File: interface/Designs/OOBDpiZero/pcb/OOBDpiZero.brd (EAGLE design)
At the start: 73.5 x 42 mm, 133 parts, among them IC1 LM1117MPX-3.3, IC11 EEPROM24, IC3 DS3231, Q2 12MHz, U1 SN65HVD230(SO8), U2 SN65HVD230(SO8), U3 MAX98357, U4 SY6280, U5 MP1482

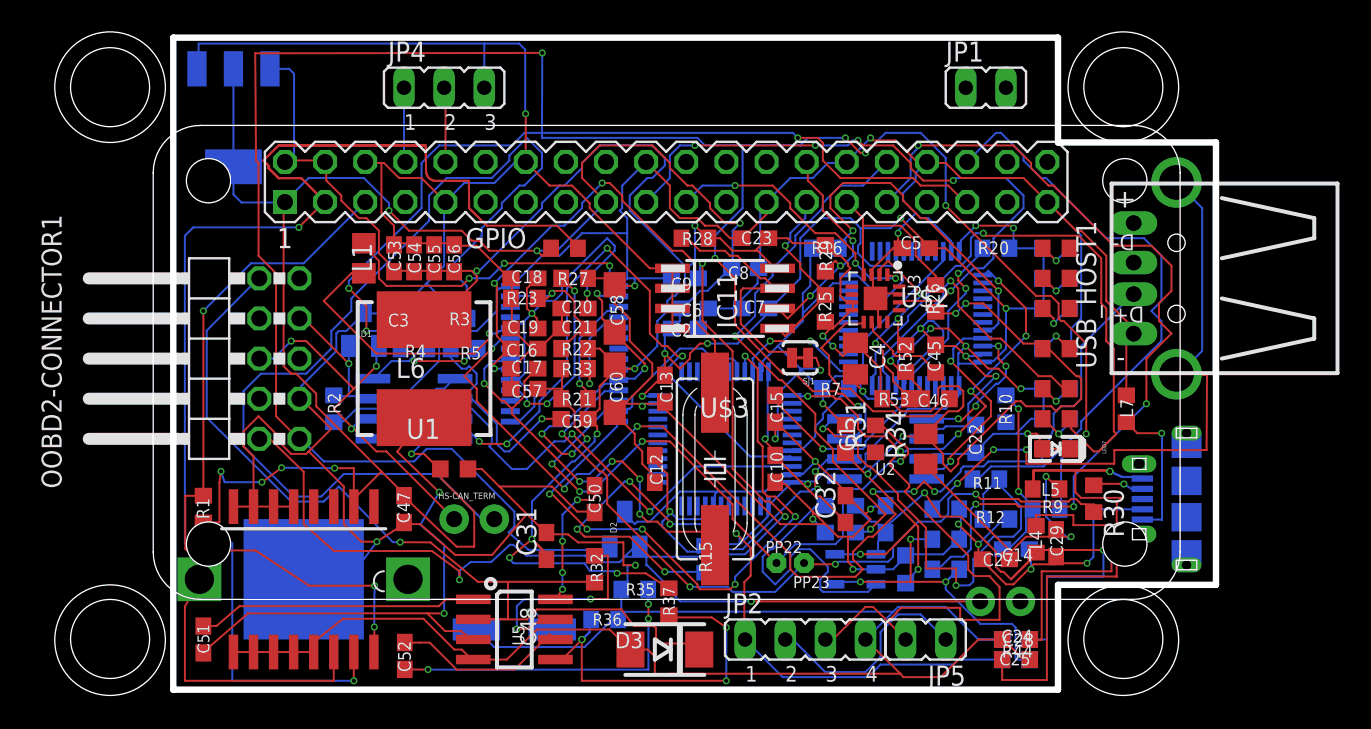
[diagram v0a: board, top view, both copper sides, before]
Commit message: 7 Lines left over, error checking in regards of overlap, distance and restriction done. Mike, please check the restrictions in regards of e.g mounting holes of the pizero pcb
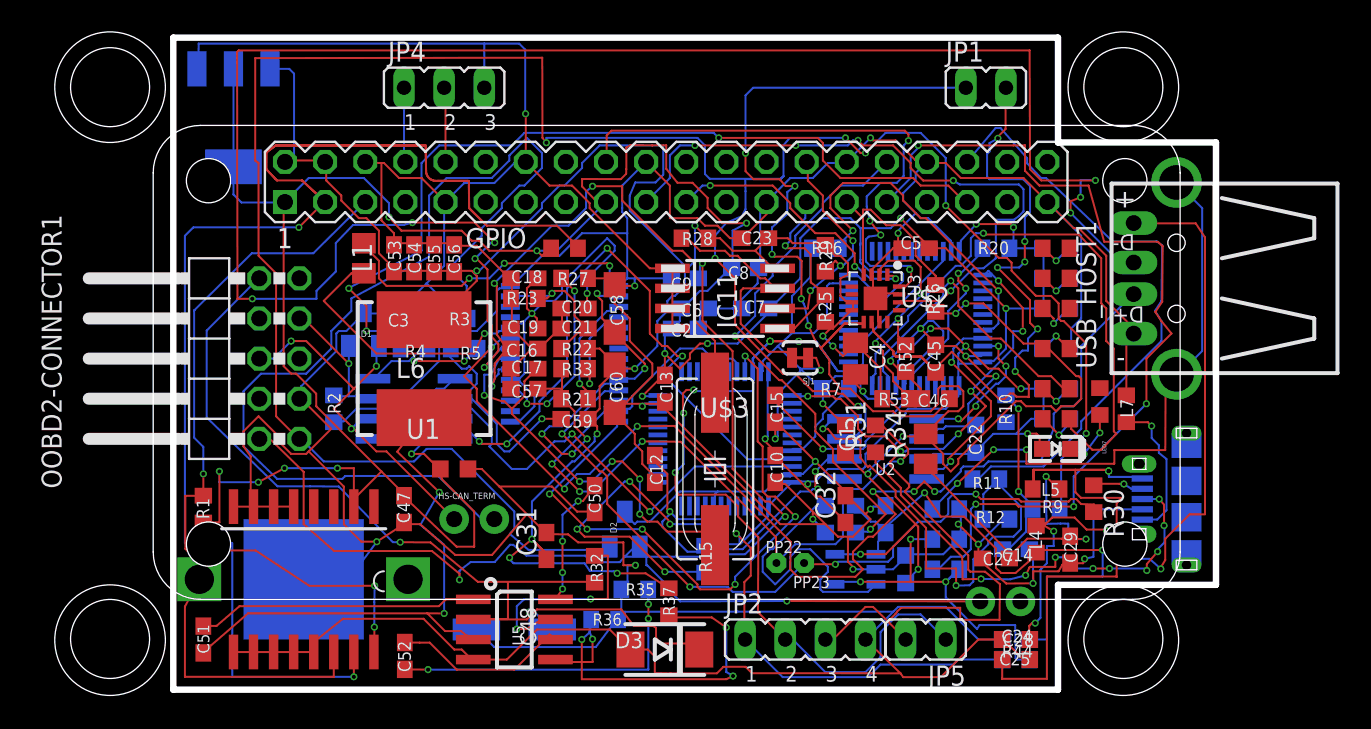
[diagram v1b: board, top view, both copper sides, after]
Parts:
- moved R18 4.08 mm to (58.6, 17.6), turned to 90 degrees
- moved C29 0.98 mm to (56.8, 8.23)
- moved C27 0.05 mm to (52.1, 7.67)
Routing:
- net USB2_DM: track 0.00 -> 118.4 mm, vias 0 -> 8
- net N$3: track 5.80 -> 46.2 mm, vias 0 -> 6
- net N$12: track 14.7 -> 53.4 mm, vias 0 -> 5
- net AUD_BCLK: track 0.00 -> 36.7 mm, vias 0 -> 4
- net SWDIO: track 32.6 -> 66.6 mm, vias 2 -> 7
- net N$43: track 0.00 -> 29.7 mm, vias 0 -> 9
- net N$41: track 18.5 -> 45.9 mm, vias 0 -> 4
- net MS-CAN_H: track 154.6 -> 159.3 mm
- net GND: track 582.3 -> 586.3 mm
- net N$42: track 40.9 -> 37.0 mm
- net +3V3: track 288.1 -> 291.5 mm
- net N$1: track 19.5 -> 21.9 mm
- net N$31: track 34.0 -> 36.4 mm
- net N$26: track 1.74 -> 3.75 mm, vias 0 -> 2
- net USB_CE: track 54.4 -> 56.4 mm
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
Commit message: 6 lines left over, design rule check made
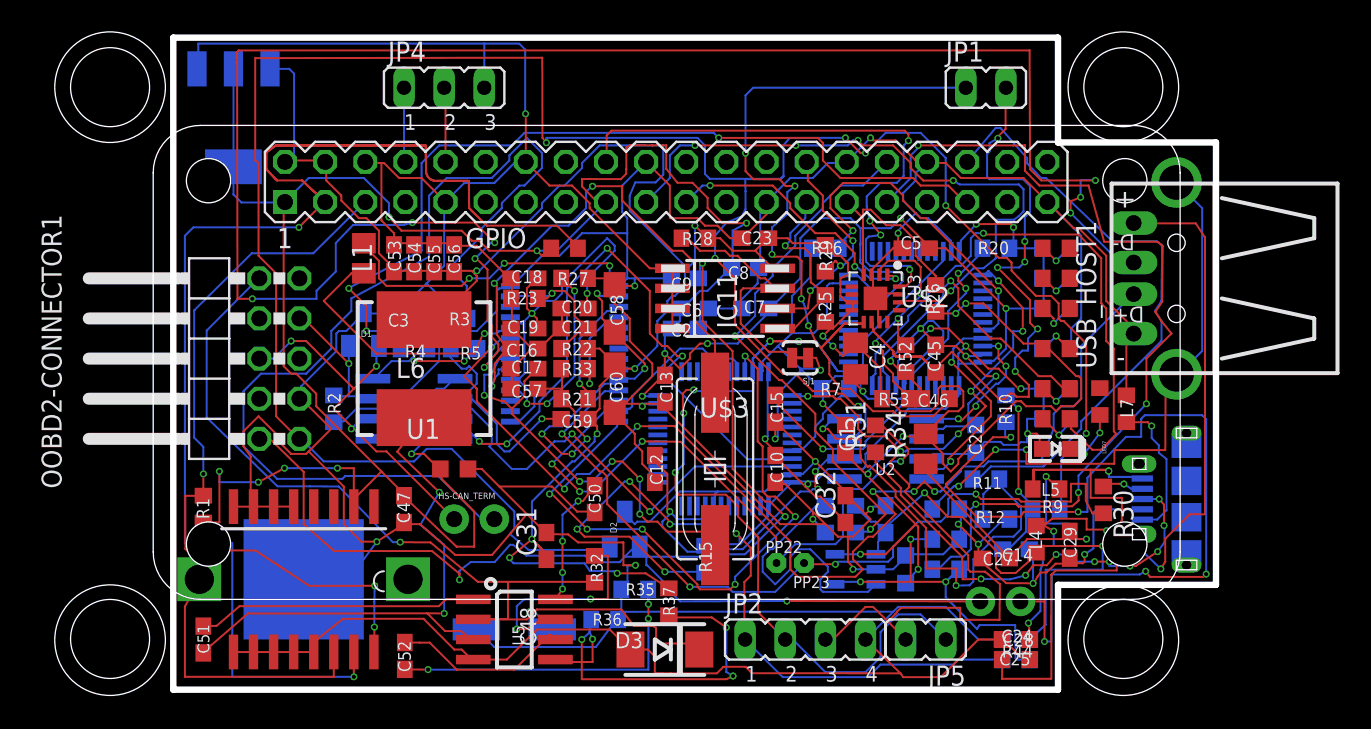
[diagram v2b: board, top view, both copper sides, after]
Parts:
- moved R30 0.61 mm to (58.9, 11.4)
- moved C29 0.31 mm to (56.7, 8.53)
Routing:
- net N$32: track 0.00 -> 57.5 mm, vias 0 -> 5
- net PP23: track 48.0 -> 50.6 mm
- net N$48: track 42.2 -> 41.2 mm
- net +3V3: track 291.5 -> 292.4 mm
- net N$47: track 34.3 -> 33.5 mm
- net N$43: track 29.7 -> 29.0 mm
- net N$38: track 3.22 -> 2.70 mm

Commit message: 4 Lines left, DRC no errors
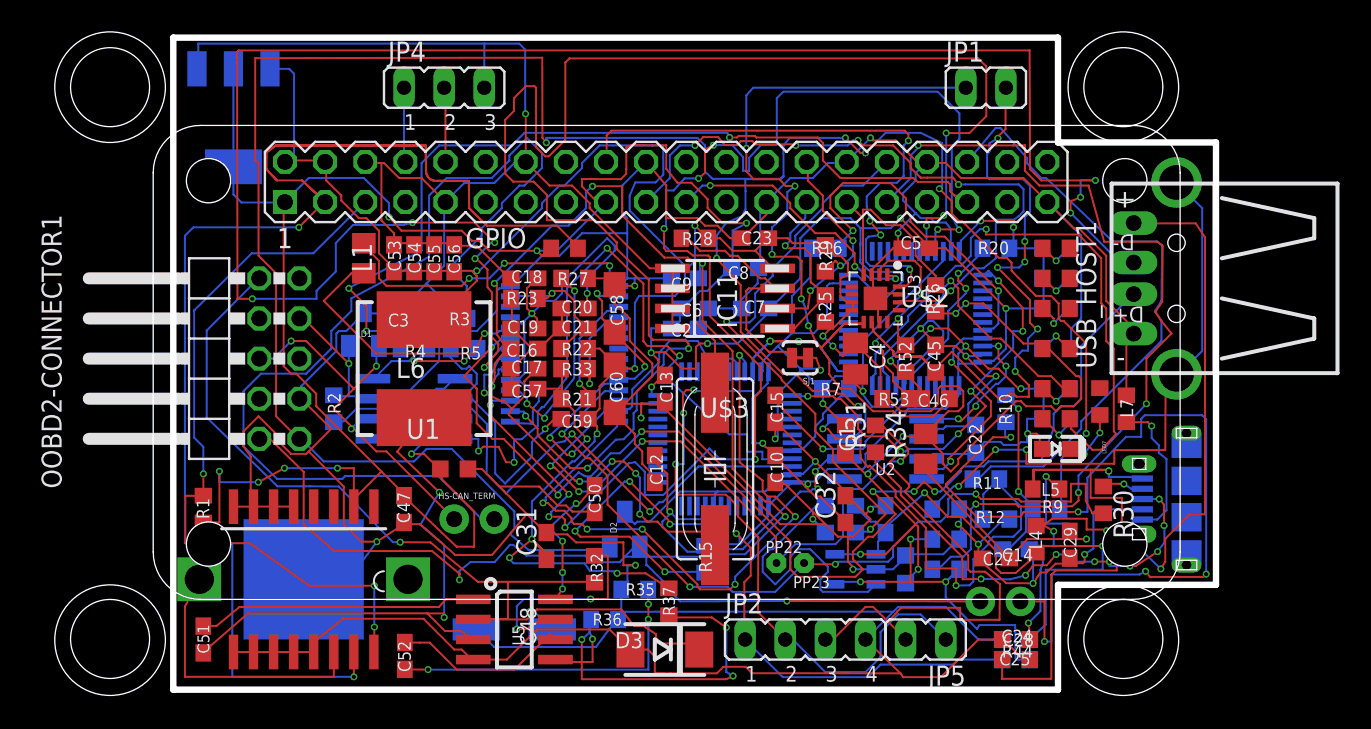
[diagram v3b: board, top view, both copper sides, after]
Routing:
- net USB1_DM: track 0.00 -> 97.2 mm, vias 0 -> 6
- net USB1_DP: track 0.00 -> 88.0 mm, vias 0 -> 10
- net GND: track 586.3 -> 592.7 mm
- net +3V3: track 292.4 -> 296.1 mm
- net HS-CAN_RXD: track 40.4 -> 43.9 mm
- net HS-CAN_TXD: track 32.3 -> 34.6 mm
- net USB0_DP: track 39.5 -> 41.0 mm
- net USB_VBUS: track 33.6 -> 34.8 mm
- net USB0_DM: track 10.5 -> 11.7 mm
- net +5V: track 189.2 -> 190.4 mm
- net N$40: track 12.1 -> 13.2 mm
- net USB2_DP: track 71.9 -> 73.0 mm
- net N$39: track 44.7 -> 45.7 mm
- net N$33: track 46.3 -> 45.4 mm
- net AUD_LRCLK: track 40.8 -> 41.6 mm
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
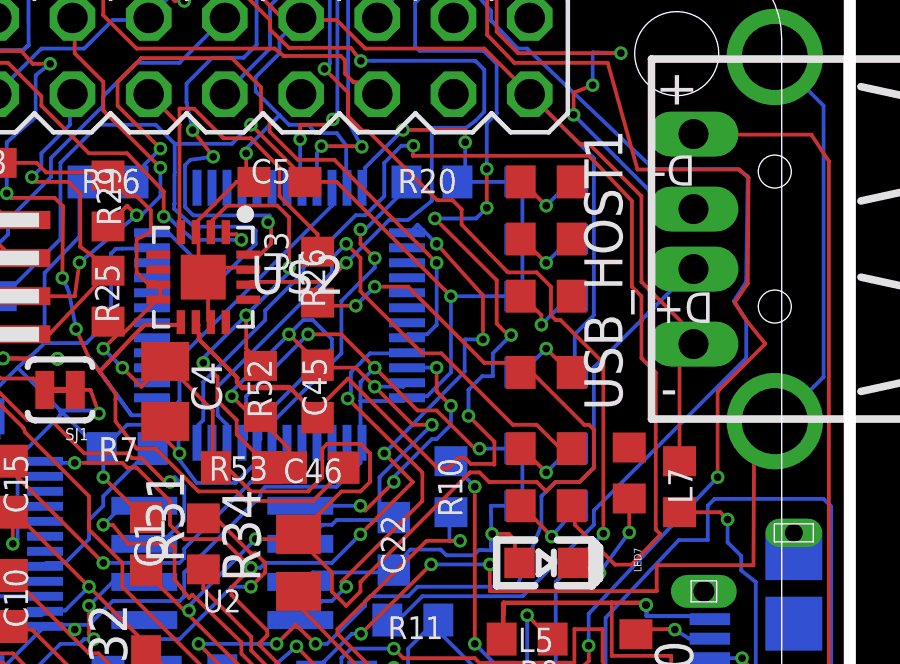
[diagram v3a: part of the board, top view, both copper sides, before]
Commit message: 3 Lines missing DRC made.
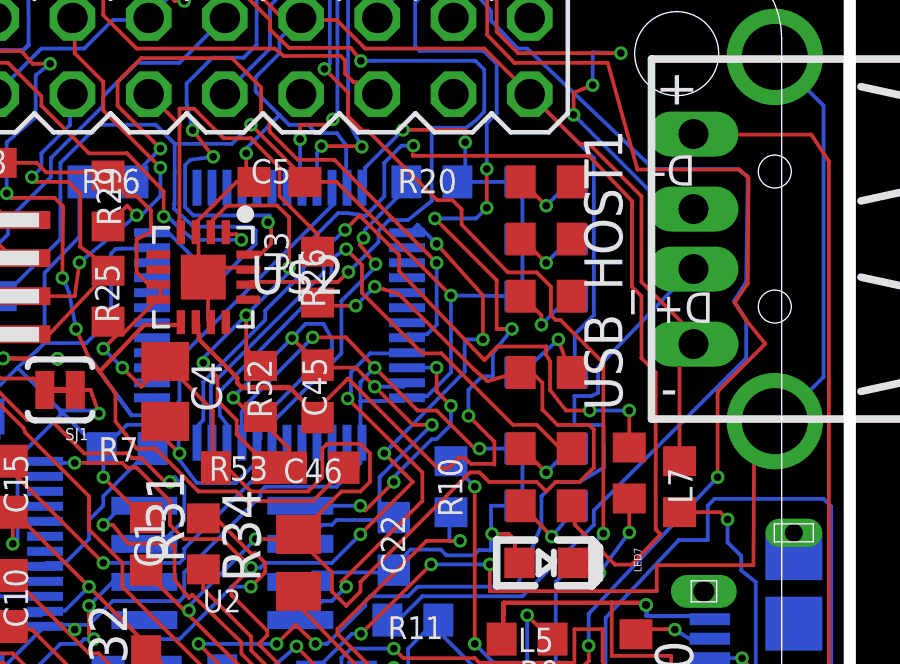
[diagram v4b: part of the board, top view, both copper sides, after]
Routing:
- net N$23: track 0.00 -> 24.1 mm, vias 0 -> 3
- net USB2_DP: track 73.0 -> 74.9 mm
- net +5V: track 190.4 -> 191.0 mm
- net N$129: track 2.40 -> 2.94 mm

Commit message: add minor modifications after schematics review
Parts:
- removed R11, R4: NI, rcl:R0603
- added JP3: 3V3 power (opt), jumper:JP1
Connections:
- new net N$50: C32.1, IC1.2, IC1.TAB, JP3.2
- net +3V3: now also JP3.1, R12.2, R5.2; no longer C32.1, IC1.2, IC1.TAB
- net GND: no longer R12.2, R5.2
- net HS-CAN_RS: no longer R4.2
- net MS-CAN_RS: no longer R11.2
- net N$5: now also U$3.2; no longer R4.1
- net N$80: now also U$2.2; no longer R11.1
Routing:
- net N$50: track 0.00 -> 11.8 mm, vias 0 -> 1
- net SDA: track 102.2 -> 91.2 mm
- net +3V3: track 295.8 -> 297.4 mm, vias 23 -> 25
